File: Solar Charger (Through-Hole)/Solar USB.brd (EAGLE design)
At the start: 74.6 x 24.1 mm, 22 parts, among them U1 MCP73871-2CCI/ML

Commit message: boost
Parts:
- removed U1: MCP73871-2CCI/ML, Microchip_By_element14_Batch_1:QFN50P400X400X100-21N
- added IC1: MCP73871, adafruit:QFN20
- C1, C2, C4: device SparkFun-Capacitors:CPOL-RADIAL-10UF-25V-KIT -> adafruit:E2,5-5
- C3: device SparkFun-Capacitors:CPOL-RADIAL-10UF-25V-KIT -> adafruit:E7,5-16
- JP1, JP2, JP3: value M023.5MM -> M02PTH; device SparkFun-Connectors:SCREWTERMINAL-3.5MM-2 -> SparkFun-Connectors:1X02
- moved THERM 43.2 mm to (14.0, 6.35), turned to 270 degrees
- moved LED1 25.4 mm to (36.8, 3.81)
- moved R4 20.4 mm to (8.89, 6.35), turned to 90 degrees
- moved C3 19.9 mm to (24.1, 11.4), turned to 180 degrees
- moved R5 18.0 mm to (11.4, 6.35), turned to 90 degrees
- moved R7 14.5 mm to (55.9, 12.7), turned to 180 degrees
- moved C1 13.7 mm to (54.6, 5.08)
- moved R3 11.7 mm to (14.0, 16.5)
- moved R2 10.9 mm to (11.4, 16.5)
- moved LED2 10.8 mm to (36.8, 11.4)
- moved R1 10.2 mm to (8.89, 16.5)
- moved R6 10.2 mm to (45.7, 17.8)
- moved JP3 10.2 mm to (59.7, 6.35)
- moved JP2 10.2 mm to (59.7, 19.1)
- moved R8 8.03 mm to (45.7, 5.08), turned to 180 degrees
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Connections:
- removed net N$6: C1.1, JP3.1, U1.14, U1.15, U1.16
- removed net N$7: C2.1, JP2.1, U1.1, U1.20
- new net N$15: C2.+, IC1.1, IC1.20, JP2.1
- new net N$17: C1.+, IC1.14, IC1.15, IC1.16, JP3.1
- net N$1: now also IC1.6, LED3.K; no longer R9.P$2, U1.5
- net N$10: now also C3.+, C4.+, IC1.17, IC1.18, IC1.19, IC1.3, IC1.4, IC1.9; no longer C3.1, C4.1, U1.17, U1.18, U1.19, U1.3, U1.4, U1.9
- net N$11: now also IC1.5, R9.P$2; no longer LED1.K, U1.8
- net N$16: now also IC1.2; no longer U1.2
- net N$2: now also C1.-, C2.-, C3.-, C4.-, IC1.10, IC1.11, IC1.21; no longer C1.2, C2.2, C3.2, C4.2, U1.10, U1.11, U1.21
- net N$3: now also IC1.12; no longer U1.12
- net N$4: now also IC1.13; no longer U1.13
- net N$8: now also IC1.7, LED2.K; no longer LED3.K, U1.6
- net N$9: now also IC1.8, LED1.K; no longer LED2.K, U1.7
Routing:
- net N$7: track 52.7 -> 0.00 mm
- net N$6: track 51.1 -> 0.00 mm, vias 1 -> 0
- net N$4: track 15.7 -> 57.9 mm
- net N$3: track 14.2 -> 50.0 mm
- net N$5: track 13.3 -> 49.0 mm
- net N$15: track 0.00 -> 24.1 mm
- net N$12: track 10.5 -> 33.6 mm
- net N$2: track 130.9 -> 109.6 mm, vias 0 -> 1
- net N$17: track 0.00 -> 19.5 mm
- net N$11: track 28.2 -> 10.2 mm, vias 0 -> 1
- net N$1: track 28.7 -> 13.5 mm
- net N$13: track 13.3 -> 27.8 mm
- net N$10: track 91.9 -> 95.2 mm
- net N$8: track 11.9 -> 8.84 mm
- net N$16: track 18.4 -> 16.4 mm, vias 1 -> 0
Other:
- board size 74.6 x 24.1 mm -> 61.9 x 22.9 mm

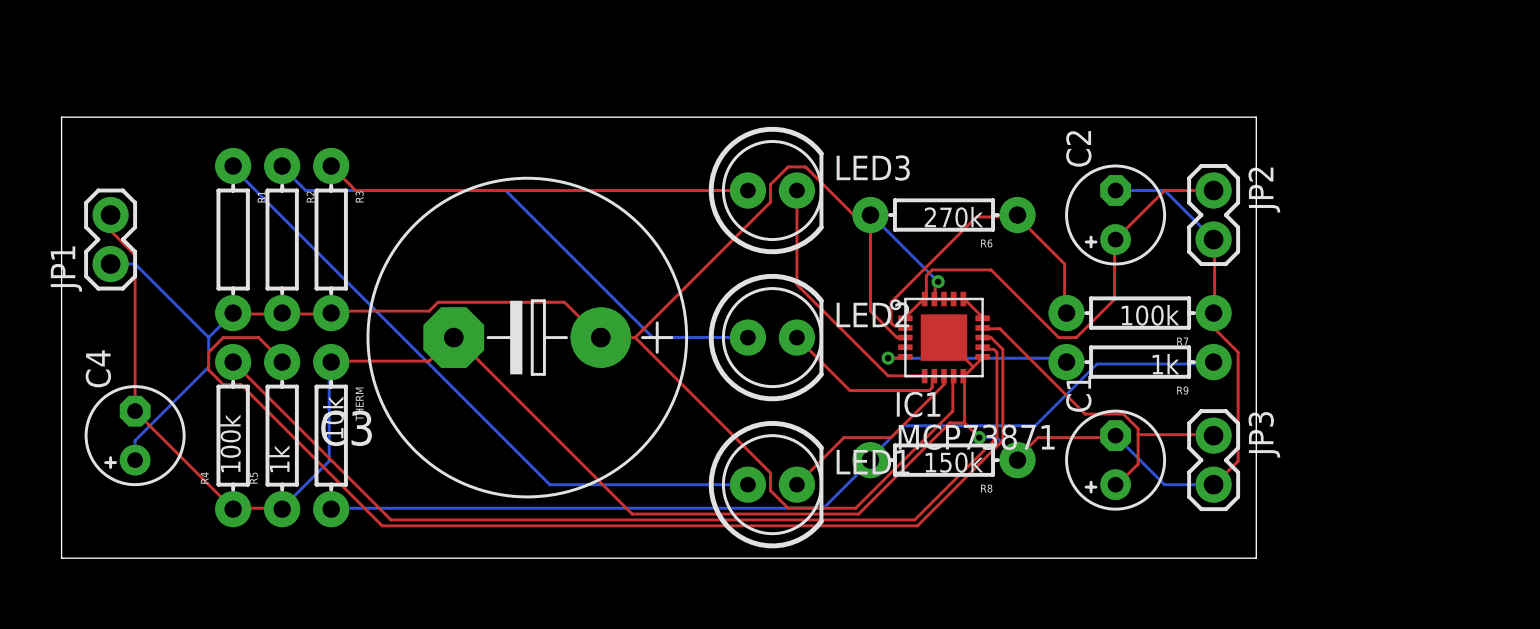
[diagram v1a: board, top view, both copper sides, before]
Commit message: Made some changes to feedback loop and reorganized controller
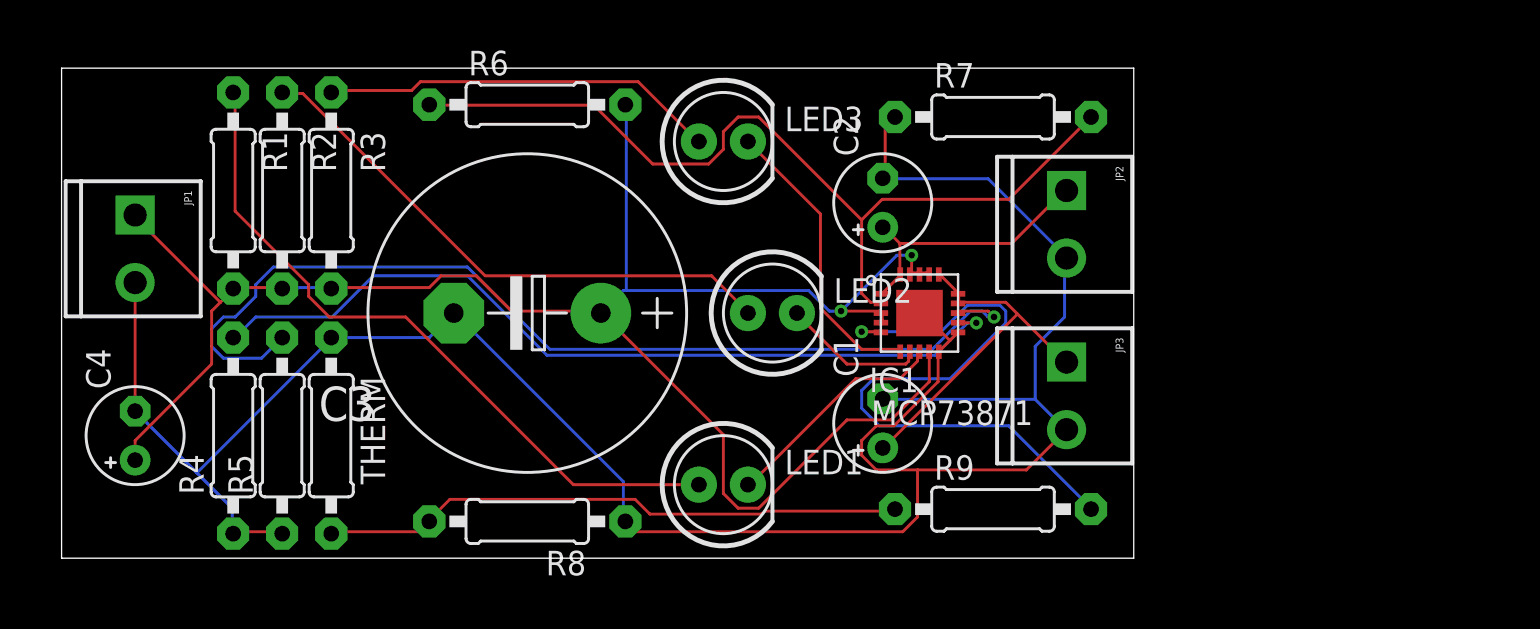
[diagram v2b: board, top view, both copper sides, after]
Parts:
- JP1, JP2, JP3: value M02PTH -> M023.5MM; device SparkFun-Connectors:1X02 -> SparkFun-Connectors:SCREWTERMINAL-3.5MM-2
- R1, R2, R3, R4, R5, R6, R7, R8, R9, THERM: device SparkFun-Resistors:AXIAL-0.3 -> adafruit:0207/10
- moved R6 22.3 mm to (24.1, 23.5), turned to 0 degrees
- moved R8 21.8 mm to (24.1, 1.91)
- moved R7 12.7 mm to (48.3, 22.9), turned to 0 degrees
- moved C1 12.2 mm to (42.5, 6.99)
- moved C2 12.1 mm to (42.5, 18.4)
- moved R9 10.8 mm to (48.3, 2.54), turned to 0 degrees
- moved JP3 8.52 mm to (52.1, 10.2)
- moved JP2 7.62 mm to (52.1, 19.1)
- moved LED3 3.59 mm to (34.3, 21.6)
- moved JP1 2.84 mm to (3.81, 17.8), turned to 270 degrees
- moved LED1 2.54 mm to (34.3, 3.81)
- moved R1 2.54 mm to (8.89, 19.1)
- moved R2 2.54 mm to (11.4, 19.1)
- moved R3 2.54 mm to (14.0, 19.1)
- moved IC1 1.80 mm to (44.5, 12.7)
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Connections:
- net N$10: now also R1.2, R2.2, R3.2, R6.2; no longer R1.P$2, R2.P$2, R3.P$2, R6.P$2
- net N$11: now also R9.2; no longer R9.P$2
- net N$12: now also R1.1; no longer R1.P$1
- net N$13: now also R2.1; no longer R2.P$1
- net N$14: now also R3.1; no longer R3.P$1
- net N$16: now also R6.1, R7.2; no longer R6.P$1, R7.P$2
- net N$2: now also R4.1, R5.1, R7.1, R8.1, THERM.1; no longer R4.P$1, R5.P$1, R7.P$1, R8.P$1, THERM.P$1
- net N$3: now also R4.2; no longer R4.P$2
- net N$4: now also R5.2; no longer R5.P$2
- net N$5: now also R8.2, R9.1, THERM.2; no longer R8.P$2, R9.P$1, THERM.P$2
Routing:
- net N$16: track 16.4 -> 46.6 mm
- net N$11: track 10.2 -> 33.7 mm
- net N$5: track 49.0 -> 30.5 mm
- net N$2: track 109.6 -> 123.2 mm, vias 1 -> 0
- net N$15: track 24.1 -> 14.0 mm
- net N$3: track 50.0 -> 43.2 mm, vias 0 -> 1
- net N$4: track 57.9 -> 52.3 mm, vias 0 -> 1
- net N$12: track 33.6 -> 36.5 mm
- net N$10: track 95.2 -> 97.5 mm, vias 1 -> 2
- net N$1: track 13.5 -> 15.3 mm
- net N$9: track 10.2 -> 12.0 mm
- net N$14: track 22.1 -> 20.6 mm
- net N$8: track 8.84 -> 7.50 mm
- net N$13: track 27.8 -> 28.9 mm
- net N$17: track 19.5 -> 18.7 mm
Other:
- board size 61.9 x 22.9 mm -> 55.5 x 25.4 mm
